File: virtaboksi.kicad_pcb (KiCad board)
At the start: 2 copper layers, 50 x 72 mm, 66 parts, among them J1 Panel_01x06, J2 External_01x06, J3 Optional_01x03, J5 Powerpole 01x02, J6 Powerpole 01x02, J7 Powerpole 01x02, J8 TagConnect_TC2030-NL, Q1 2N7002, Q10 MMBT3906, Q11 MMBT3906, Q12 MMBT3906, Q13 MMBT3906, Q2 IRF4905, Q3 IRF4905, Q4 2N7002, Q5 IRF4905, Q6 IRF4905, Q7 2N7002, Q8 IRF4905, Q9 IRF4905, U1 SRV05-4, U2 AMSRI-783.3-NZ, U3 SRV05-4, U4 SP3485EN, U5 STM8S003F3P

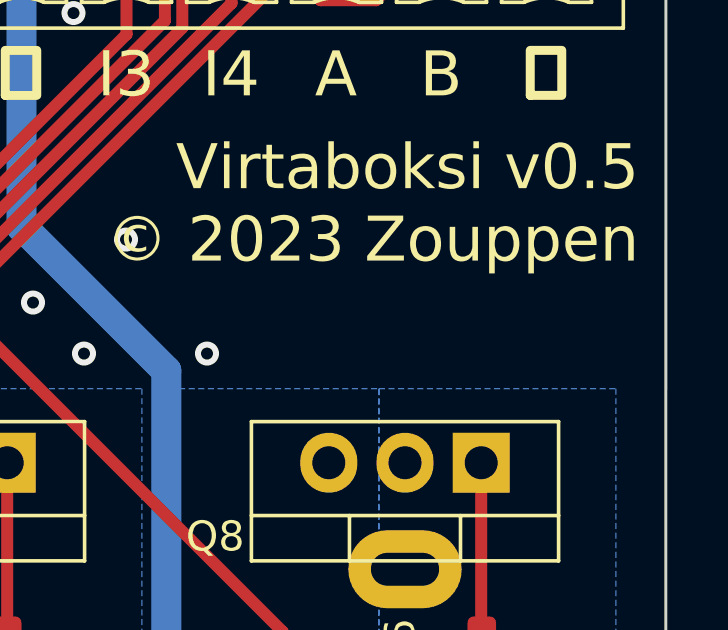
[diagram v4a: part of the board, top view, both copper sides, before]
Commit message: Add JLCPCB order number to a predefined spot
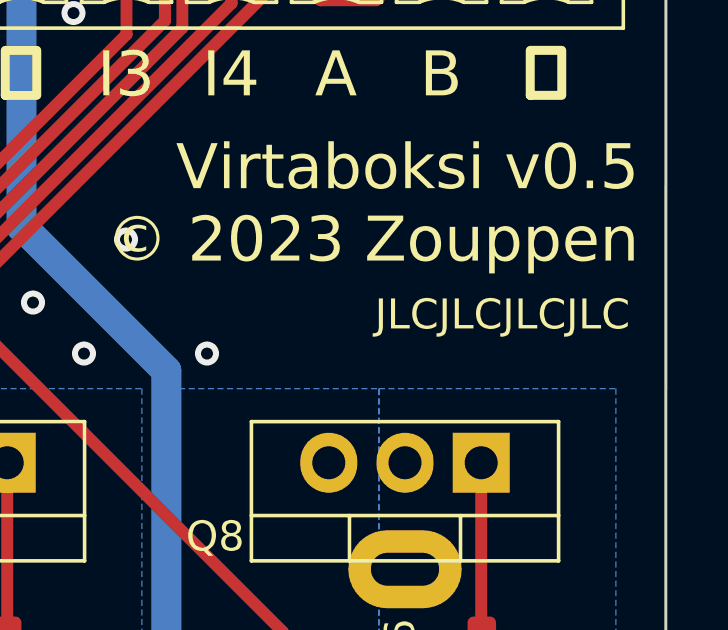
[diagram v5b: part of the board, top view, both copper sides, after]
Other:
- board text added: "JLCJLCJLCJLC"
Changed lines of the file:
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@@
     (effects (font (size 1 1) (thickness 0.25)))
+  )
+  (gr_text "JLCJLCJLCJLC" (at 154.8 61.4) (layer "F.SilkS")
+    (effects (font (size 1 1) (thickness 0.15)) (justify right))
   )
   (gr_text "O2" (at 120.5 53.4) (layer "F.SilkS")

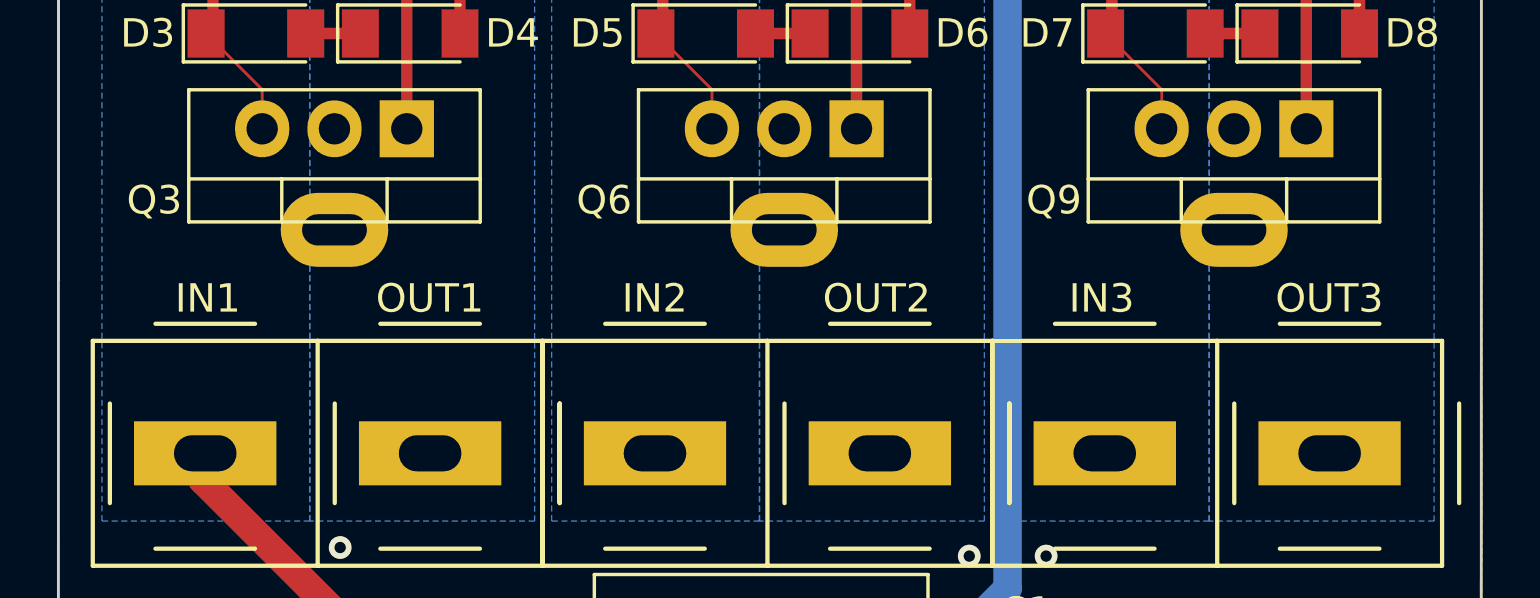
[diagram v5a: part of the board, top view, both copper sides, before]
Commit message: Rename IN1..3 as Gn IN and OUT1..3 Gn OUT on silkscreen
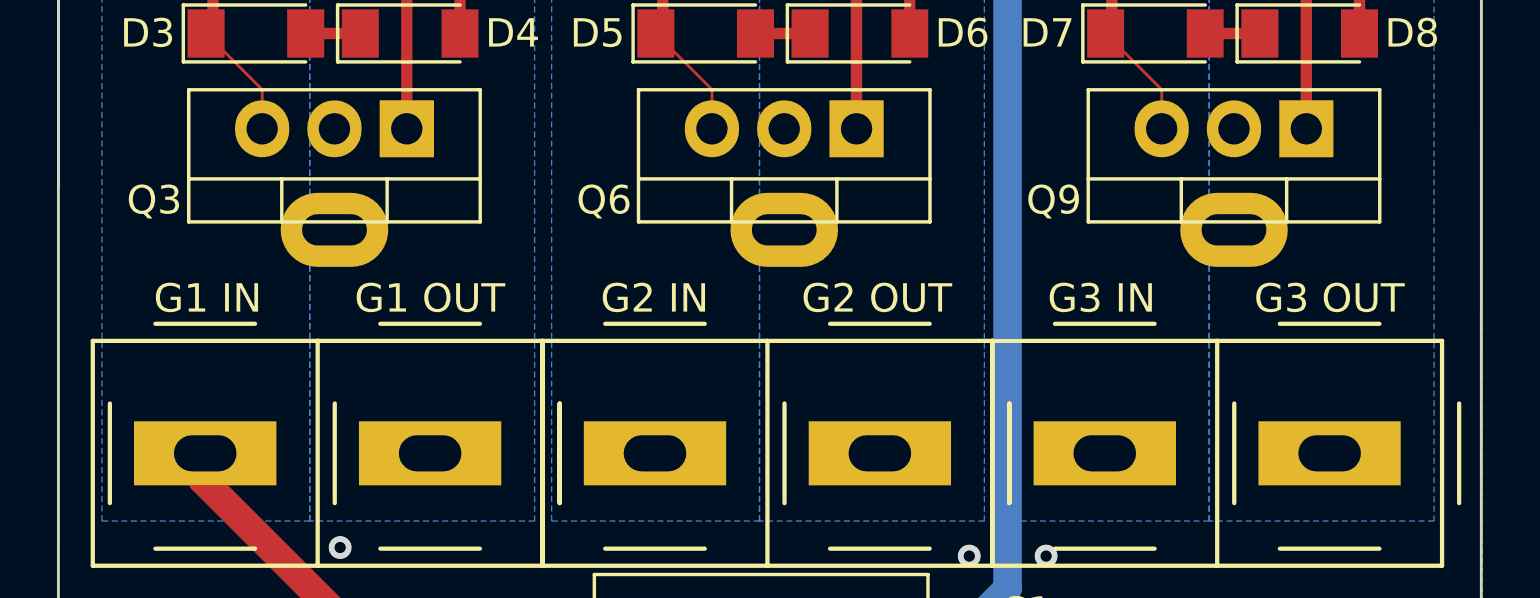
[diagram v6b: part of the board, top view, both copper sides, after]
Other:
- board text added: "G1 IN"
- board text added: "G1 OUT"
- board text added: "G2 IN"
- board text added: "G2 OUT"
- board text added: "G3 IN"
- board text added: "G3 OUT"
- board text removed: "IN1"
- board text removed: "IN2"
- board text removed: "IN3"
- board text removed: "OUT1"
- board text removed: "OUT2"
- board text removed: "OUT3"
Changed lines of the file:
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@@
     (effects (font (size 1.5 1.5) (thickness 0.3)))
   )
-  (gr_text "OUT3" (at 150.65 87.95) (layer "F.SilkS")
+  (gr_text "G3 OUT" (at 150.65 87.95) (layer "F.SilkS")
     (effects (font (size 1 1) (thickness 0.25)))
   )
@@
     (effects (font (size 1.5 1.5) (thickness 0.3)))
   )
-  (gr_text "IN3" (at 142.65 87.95) (layer "F.SilkS")
+  (gr_text "G3 IN" (at 142.65 87.95) (layer "F.SilkS")
     (effects (font (size 1 1) (thickness 0.25)))
   )
@@
     (effects (font (size 1.5 1.5) (thickness 0.3)))
   )
-  (gr_text "IN1" (at 111.25 87.95) (layer "F.SilkS")
+  (gr_text "G1 IN" (at 111.25 87.95) (layer "F.SilkS")
     (effects (font (size 1 1) (thickness 0.25)))
   )
-  (gr_text "OUT1" (at 119.05 87.95) (layer "F.SilkS")
+  (gr_text "G1 OUT" (at 119.05 87.95) (layer "F.SilkS")
     (effects (font (size 1 1) (thickness 0.25)))
   )
@@
     (effects (font (size 1.5 1.5) (thickness 0.3)))
   )
-  (gr_text "IN2" (at 126.95 87.95) (layer "F.SilkS")
+  (gr_text "G2 IN" (at 126.95 87.95) (layer "F.SilkS")
     (effects (font (size 1 1) (thickness 0.25)))
   )
-  (gr_text "OUT2" (at 134.75 87.95) (layer "F.SilkS")
+  (gr_text "G2 OUT" (at 134.75 87.95) (layer "F.SilkS")
     (effects (font (size 1 1) (thickness 0.25)))
   )

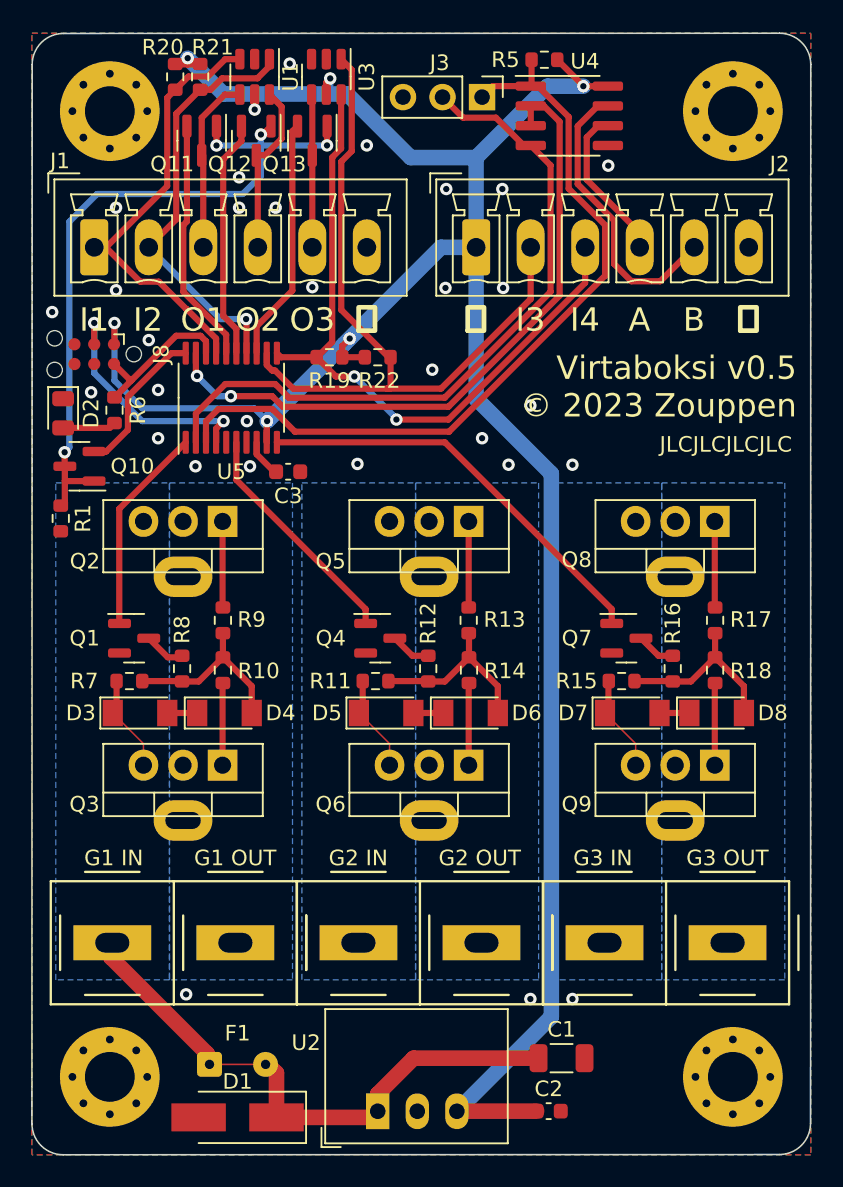
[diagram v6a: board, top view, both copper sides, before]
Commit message: Reorganize pins so that we got two analog inputs, bot I1 and I2
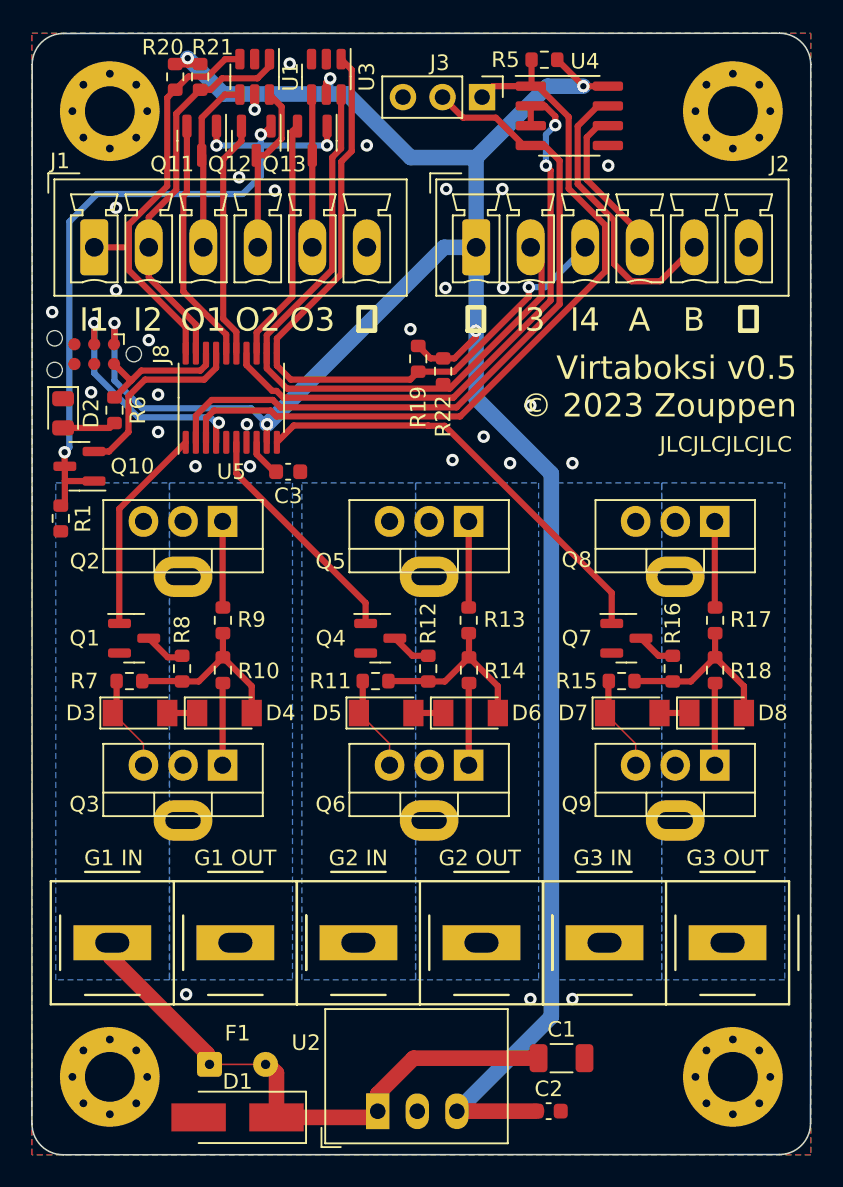
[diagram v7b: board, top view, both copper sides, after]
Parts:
- moved R19 5.70 mm to (130.8, 55.9), turned to -90 degrees
- moved R22 4.30 mm to (132.4, 56.7), turned to -90 degrees
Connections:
- U3 pad 1: /IN3 -> /IN4
- U3 pad 6: /IN4 -> /IN3
- U5 pad 14: /IN2 -> /TX_EN
- U5 pad 17: /IN1 -> /IREF_EN
- U5 pad 19: /TX_EN -> /IN2
- U5 pad 20: /IREF_EN -> /IN1
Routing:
- net /TX_EN: track 43.3 -> 39.1 mm
- net /IN3: track 47.3 -> 44.1 mm
- net /IN1: track 29.7 -> 26.9 mm
- net /IREF_EN: track 10.00 -> 12.4 mm
- net /IN2: track 27.4 -> 25.1 mm, vias 1 -> 0
- net /GROUP3 CTRL: track 26.9 -> 28.4 mm
- net /TX: track 45.5 -> 46.9 mm
- net +3.3V: track 149.6 -> 150.9 mm
- net /IN4: track 45.0 -> 46.0 mm, vias 2 -> 1
- net /RX: track 51.5 -> 50.6 mm
- net /SWIM: track 9.98 -> 9.05 mm
- net /RESET: track 15.7 -> 15.0 mm
- net GND: vias 30 -> 28

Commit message: Mosfet drive clearances larger, update comments
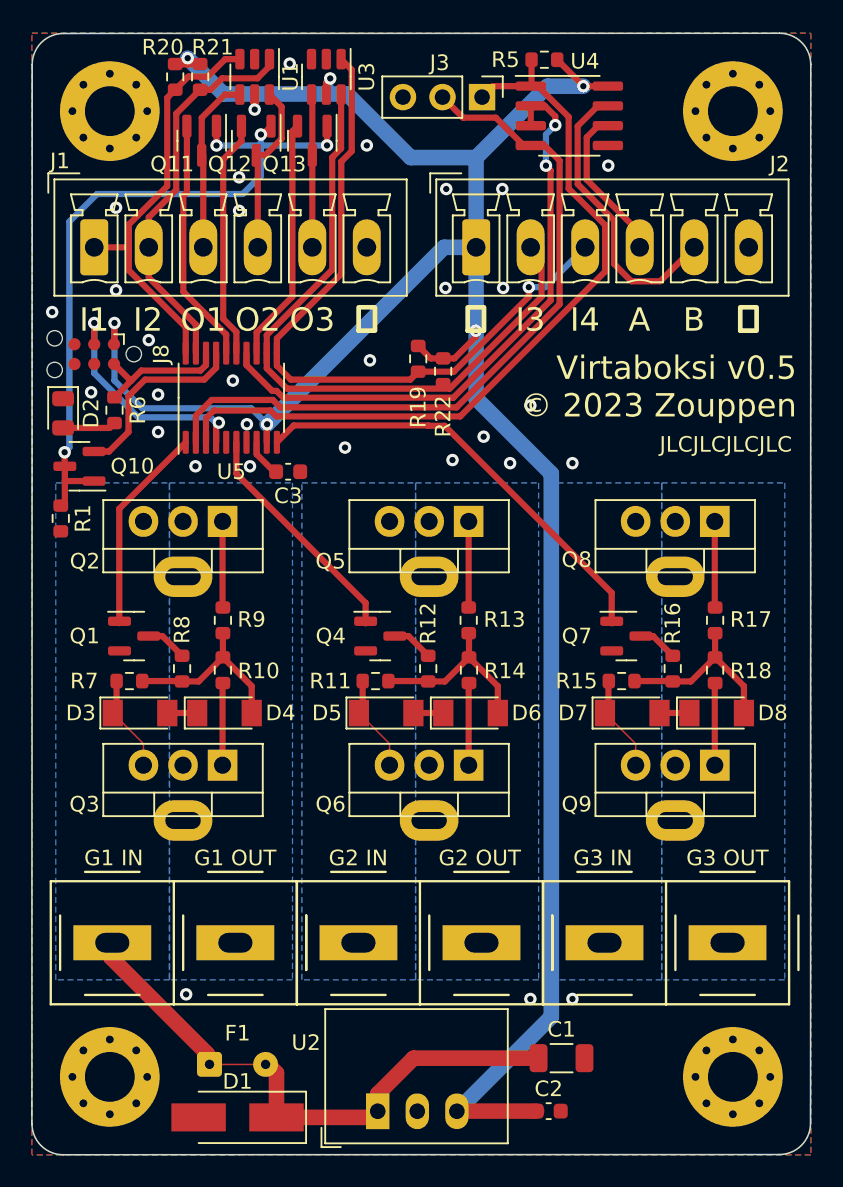
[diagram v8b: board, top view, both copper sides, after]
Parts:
- moved Q1 0.14 mm to (112.6, 73.7)
- moved Q4 0.14 mm to (128.4, 73.7)
- moved Q7 0.14 mm to (144.2, 73.7)
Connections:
- net Net-(D4-Pad2) renamed /mosfet_switch1/DRIVE
- net Net-(D6-Pad2) renamed /mosfet_switch2/DRIVE
- net Net-(D8-Pad2) renamed /mosfet_switch3/DRIVE
- net Net-(Q2-Pad1) renamed /mosfet_switch1/DRIVE_A
- net Net-(Q3-Pad1) renamed /mosfet_switch1/DRIVE_B
- net Net-(Q5-Pad1) renamed /mosfet_switch2/DRIVE_A
- net Net-(Q6-Pad1) renamed /mosfet_switch2/DRIVE_B
- net Net-(Q8-Pad1) renamed /mosfet_switch3/DRIVE_A
- net Net-(Q9-Pad1) renamed /mosfet_switch3/DRIVE_B
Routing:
- net GND: vias 28 -> 30
